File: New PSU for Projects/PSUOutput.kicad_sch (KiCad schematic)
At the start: 47 parts, among them IC1 IRS21867STRPBF, IC2 IRS21867STRPBF, IC3 MCP6022-I_SN, Q1 BC848, Q2 BC848, Q3 IRFR2905ZTRPBF, Q4 IRFR2905ZTRPBF, Q5 IRFR2905ZTRPBF, Q6 IRFR2905ZTRPBF

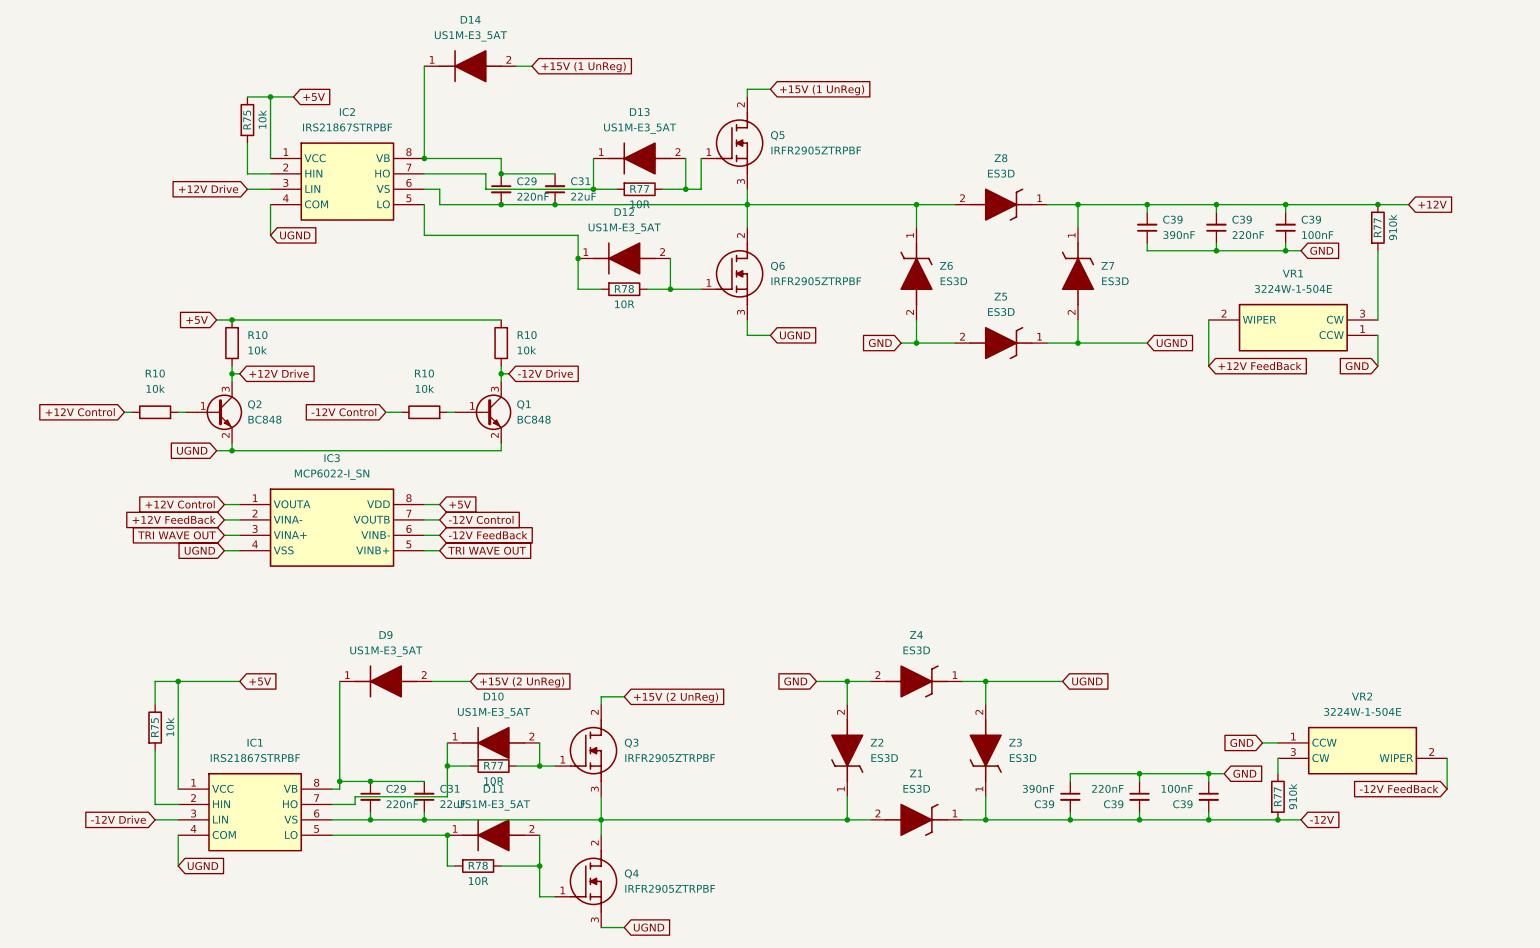
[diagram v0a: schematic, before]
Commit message: Swapped out Op-Amp for a Comparator
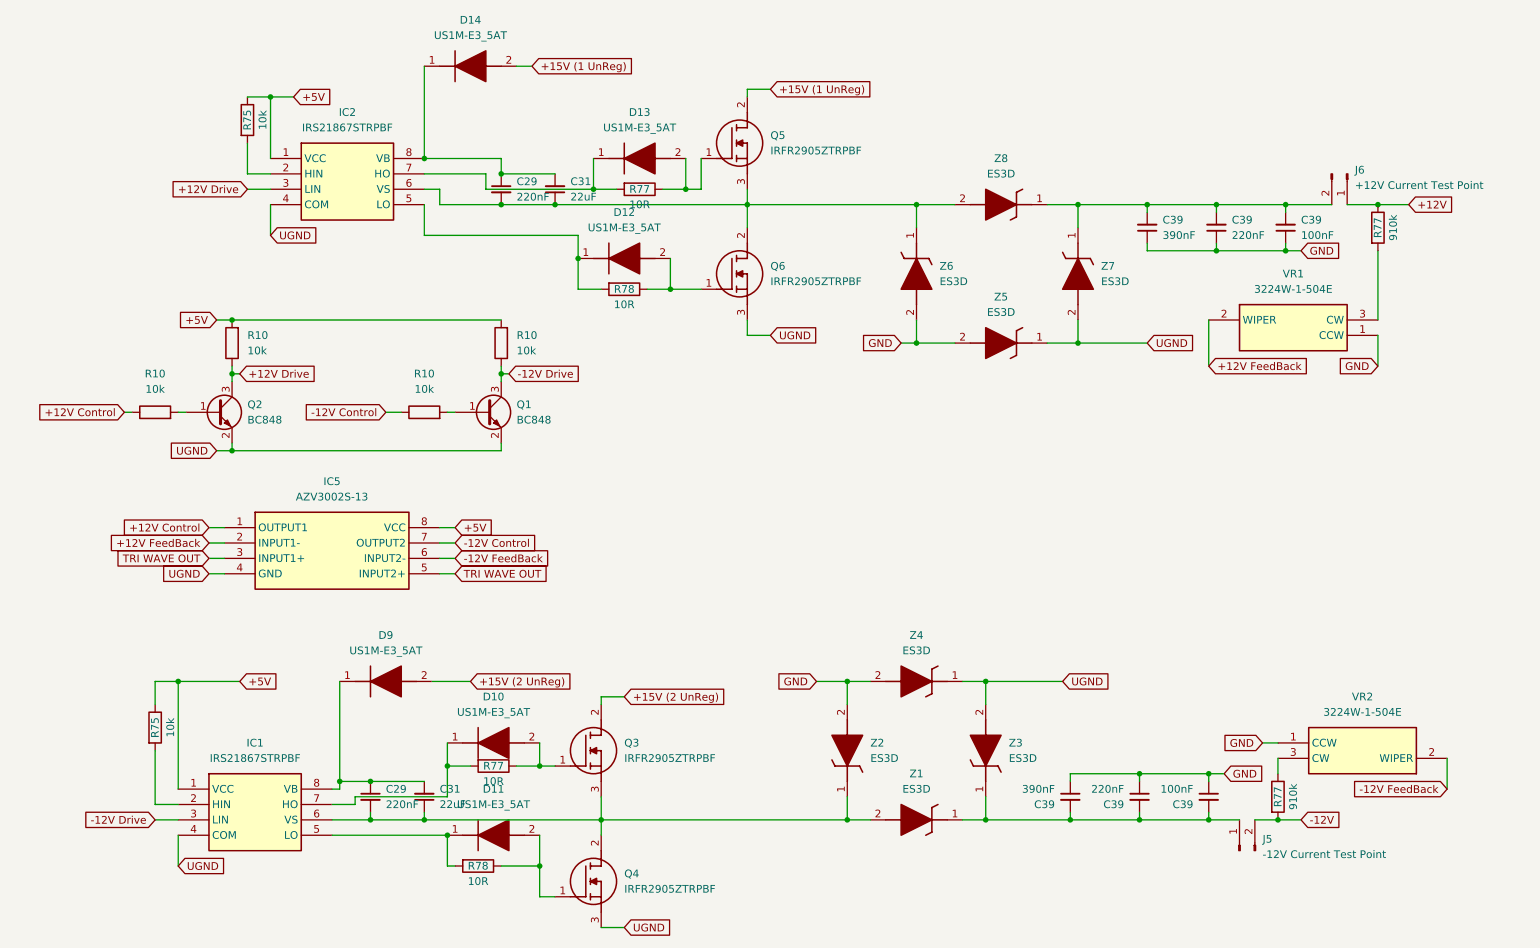
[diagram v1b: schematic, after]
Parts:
- removed IC3: MCP6022-I_SN, SOIC127P600X175-8N, symbol SamacSys_Parts:MCP6022-I_SN
- added IC5: AZV3002S-13, SOIC127P600X175-8N, symbol SamacSys_Parts:AZV3002S-13
- added J5: -12V Current Test Point, symbol Connector:Conn_01x02_Pin
- added J6: +12V Current Test Point, symbol Connector:Conn_01x02_Pin
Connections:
- net +12V: now also J6.1 (Pin_1); no longer C39.2, C39.2, C39.2, Z7.1 (K), Z8.1 (K)
- net +12V Control: now also IC5.1 (OUTPUT1)
- net +12V FeedBack: now also IC5.2 (INPUT1-)
- net +5V: now also IC5.8 (VCC)
- net -12V: now also J5.2 (Pin_2); no longer C39.2, C39.2, C39.2, Z1.1 (K), Z3.1 (K)
- net -12V Control: now also IC5.7 (OUTPUT2)
- net -12V FeedBack: now also IC5.6 (INPUT2-)
- net TRI WAVE OUT: now also IC5.3 (INPUT1+), IC5.5 (INPUT2+)
- net UGND: now also IC5.4 (GND)
- new net: C39.2, C39.2, C39.2, J5.1 (Pin_1), Z1.1 (K), Z3.1 (K)
- new net: C39.2, C39.2, C39.2, J6.2 (Pin_2), Z7.1 (K), Z8.1 (K)

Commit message: Minor Change to feedback circuit
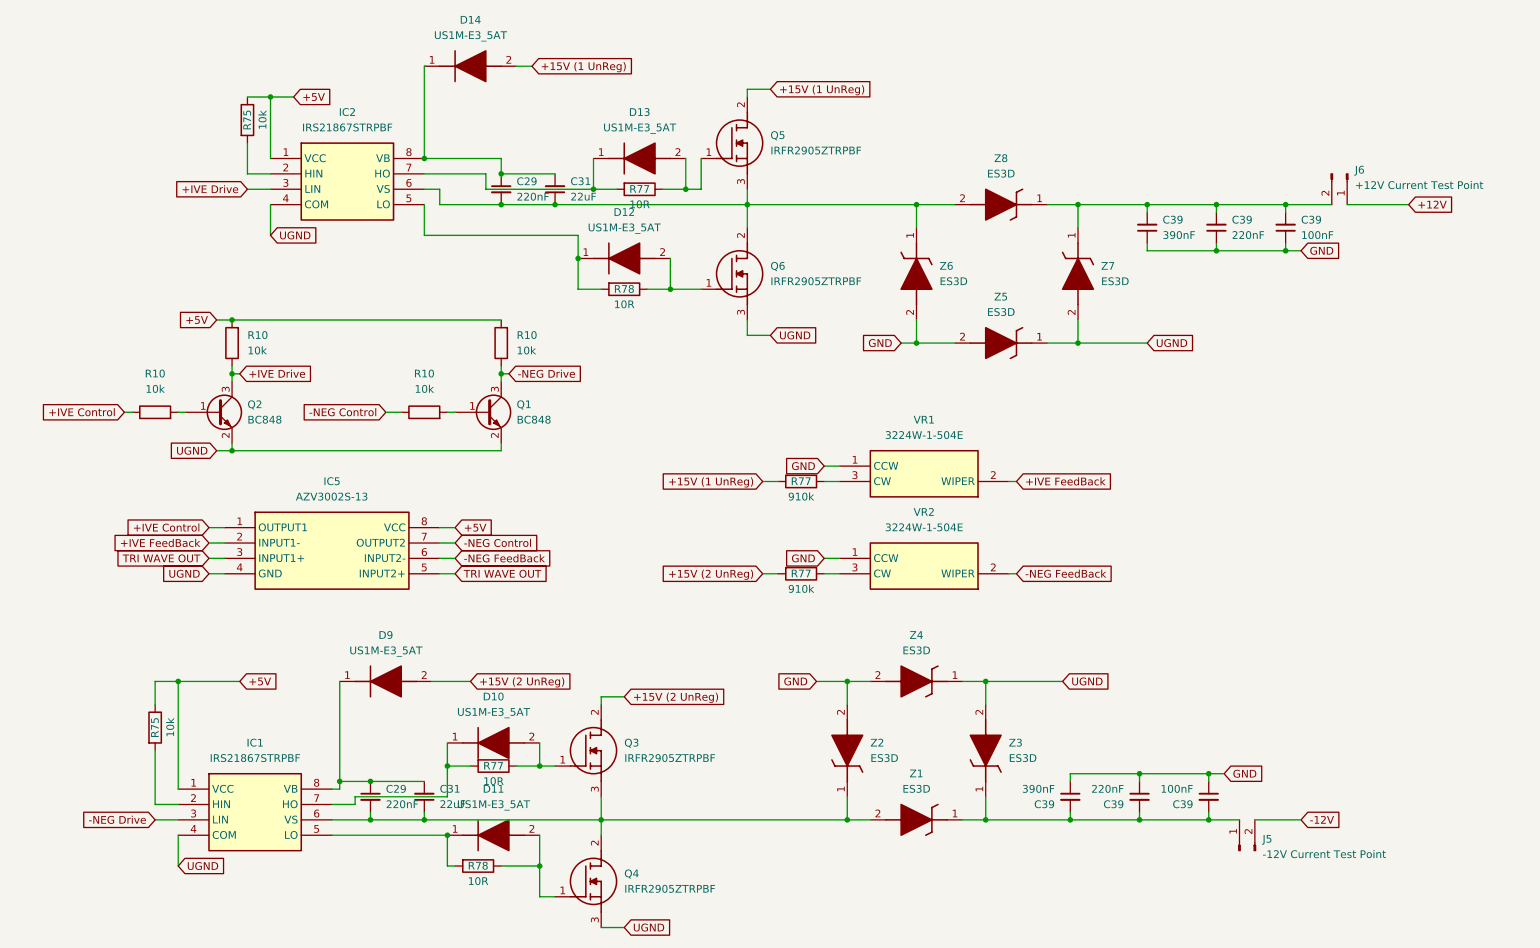
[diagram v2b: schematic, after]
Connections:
- net +12V: no longer R77.1
- net +15V (1 UnReg): now also R77.2
- net +15V (2 UnReg): now also R77.2
- net -12V: no longer R77.2
- net at VR1.3 (CW): now also R77.1; no longer R77.2
- net +12V Control renamed +IVE Control
- net +12V Drive renamed +IVE Drive
- net +12V FeedBack renamed +IVE FeedBack
- net -12V Control renamed -NEG Control
- net -12V Drive renamed -NEG Drive
- net -12V FeedBack renamed -NEG FeedBack
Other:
- moved on the sheet: R77, VR1, VR2

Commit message: A few minor changes
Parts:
- removed J5: -12V Current Test Point, symbol Connector:Conn_01x02_Pin
- removed J6: +12V Current Test Point, symbol Connector:Conn_01x02_Pin
- removed Z1, Z2, Z3, Z4, Z5, Z6, Z7, Z8: ES3D, DIOM8059X265N, symbol SamacSys_Parts:ES3D
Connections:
- net +12V: now also C29.2, C31.1, C39.2, C39.2, C39.2, IC2.6 (VS), Q5.3 (S), Q6.2 (D)
- net -12V: now also C29.2, C31.1, C39.2, C39.2, C39.2, IC1.6 (VS), Q3.3 (S), Q4.2 (D)
- net GND: no longer VR1.1 (CCW), VR2.1 (CCW)
- net UGND: now also VR1.1 (CCW), VR2.1 (CCW)
- net +15V (2 UnReg) renamed -15V (2 UnReg)
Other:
- moved on the sheet: C39
